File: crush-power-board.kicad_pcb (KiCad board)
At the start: 4 copper layers, 105 parts, among them J1 XT90PW-F, J2 1x2 Header, J3 Molex Micro Fit 3.0, J4 Barrel_Jack, J5 2157601008, U1 BD9G341AEFJ, U2 SIC461ED-T1-GE3, U3 SIC461ED-T1-GE3, U4 BD9G341AEFJ

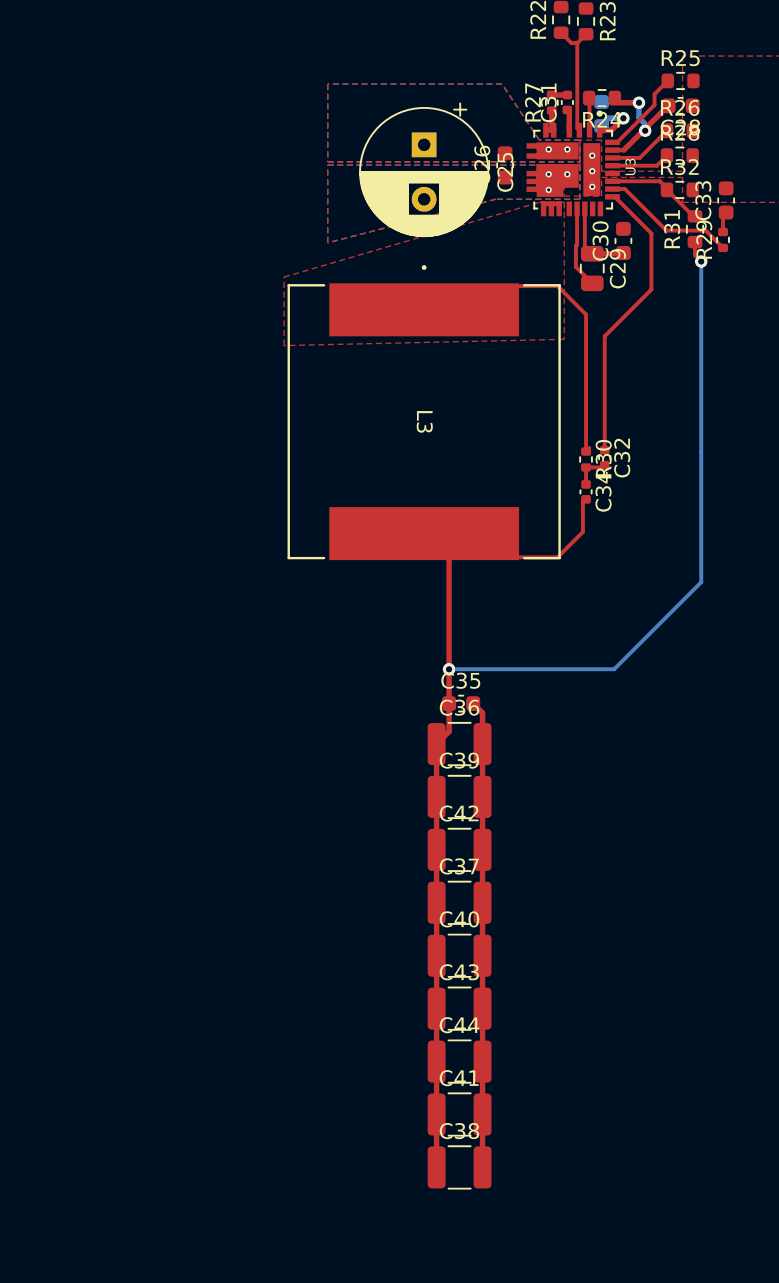
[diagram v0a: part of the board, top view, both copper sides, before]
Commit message: Added more vias and plane differences to 5V reg
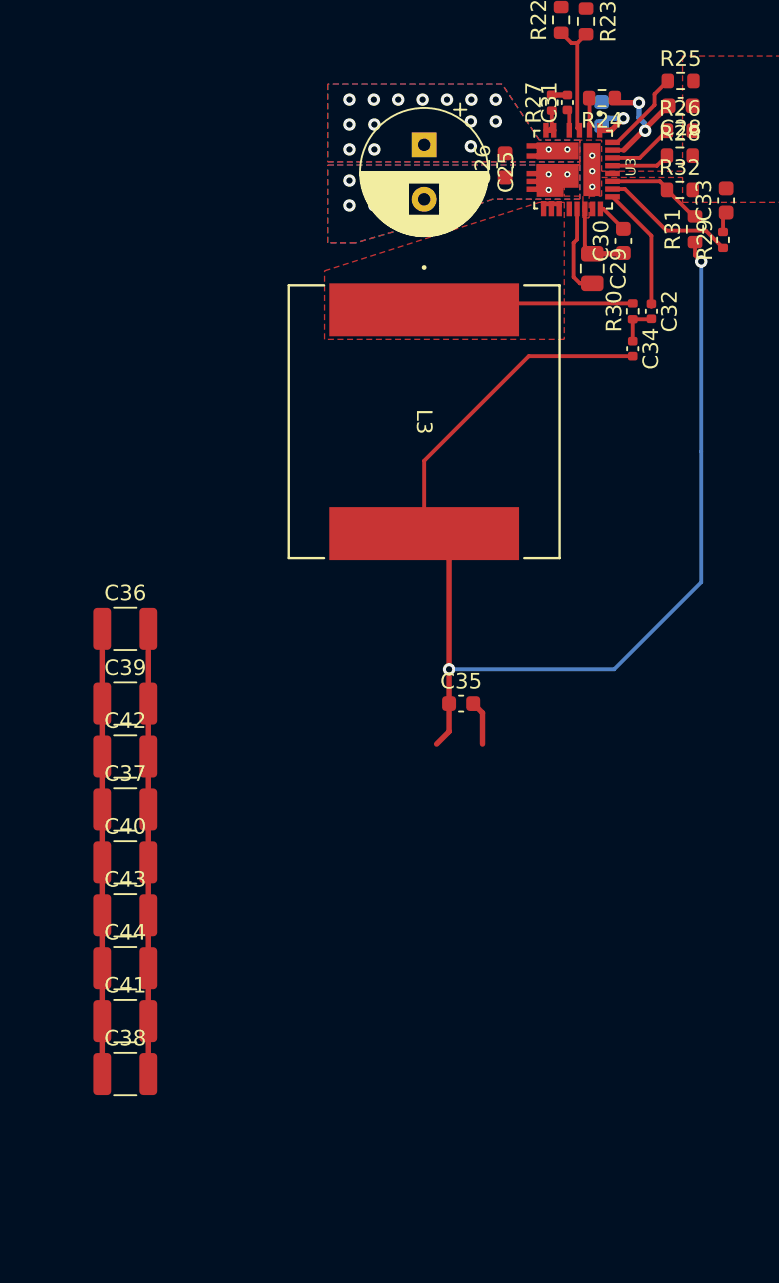
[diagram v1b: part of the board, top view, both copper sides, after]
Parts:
- moved C36 22.7 mm to (119.4, 105.0)
- moved C44 22.3 mm to (119.4, 126.8)
- moved C37 22.3 mm to (119.4, 116.6)
- moved C38 22.3 mm to (119.4, 133.6)
- moved C39 22.3 mm to (119.4, 109.8)
- moved C40 22.3 mm to (119.4, 120.0)
- moved C41 22.3 mm to (119.4, 130.2)
- moved C42 22.3 mm to (119.4, 113.2)
- moved C43 22.3 mm to (119.4, 123.4)
- moved R30 9.98 mm to (152.0, 84.6)
- moved C32 9.87 mm to (153.2, 84.6)
- moved C34 9.68 mm to (152.0, 87.0)
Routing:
- net Net-(U3-VSNS): track 18.6 -> 8.11 mm
- net 5V: track 96.1 -> 103.4 mm
- net Net-(L3-Pad1): track 20.7 -> 13.6 mm
- net Net-(U3-SS): track 0.00 -> 2.01 mm
- net Net-(U3-VDRV): track 5.25 -> 5.84 mm
- net GND: vias 31 -> 37
- net +BATT: vias 4 -> 18

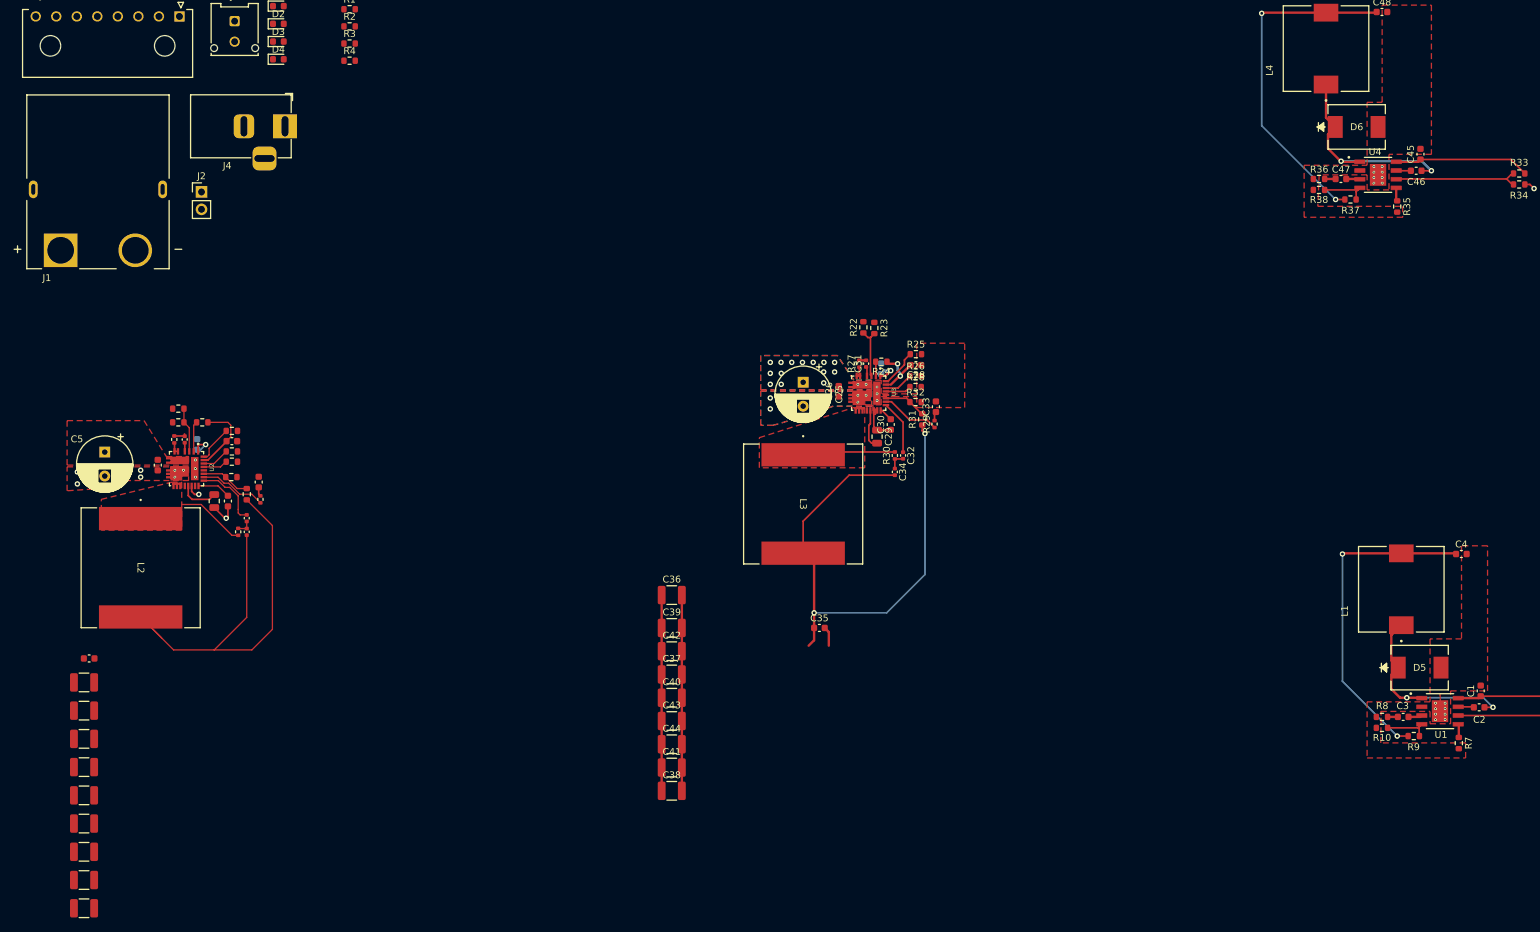
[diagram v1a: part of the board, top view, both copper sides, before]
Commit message: start 12v routing
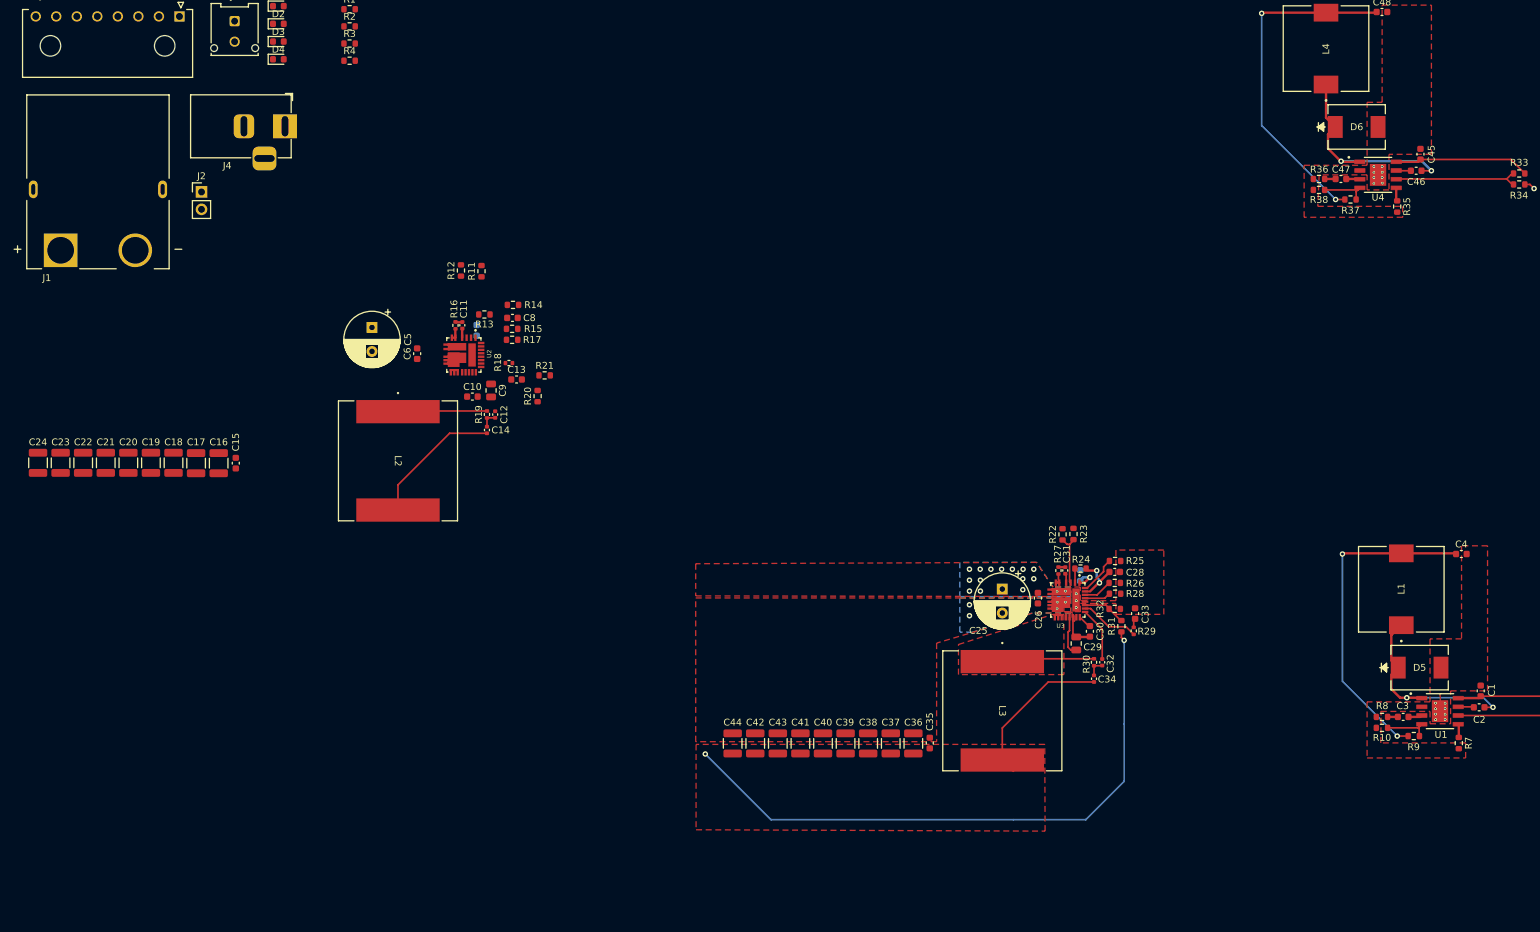
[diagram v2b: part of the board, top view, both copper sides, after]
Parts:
- moved C22 65.1 mm to (33.4, 85.7), turned to 90 degrees
- moved C23 61.1 mm to (30.1, 85.7), turned to 90 degrees
- moved C24 57.2 mm to (26.8, 85.7), turned to 90 degrees
- moved C19 53.6 mm to (43.3, 85.7), turned to 90 degrees
- moved R11 49.5 mm to (91.6, 57.7), turned to 90 degrees
- moved C20 49.0 mm to (40.0, 85.7), turned to 90 degrees
- moved R21 48.1 mm to (100.8, 72.9)
- moved R12 46.0 mm to (88.6, 57.6), turned to 90 degrees
- moved R14 45.0 mm to (96.2, 62.6)
- moved R20 44.9 mm to (99.8, 75.9)
- moved C16 44.8 mm to (53.2, 85.7), turned to 90 degrees
- moved C8 44.8 mm to (96.1, 64.5)
- moved R15 44.7 mm to (96.1, 66.1)
- moved R17 44.7 mm to (96.1, 67.7)
- moved C21 44.6 mm to (36.7, 85.7), turned to 90 degrees
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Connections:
- U1 pad 9: GND -> (no net)
- U4 pad 9: GND1 -> (no net)
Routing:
- net 12V: track 66.0 -> 19.8 mm
- net GND: track 47.4 -> 10.9 mm, vias 37 -> 21
- net Net-(U2-VDD): track 10.6 -> 0.00 mm
- net Net-(U2-COMP): track 9.83 -> 0.00 mm
- net Net-(U2-VSNS): track 9.81 -> 0.00 mm
- net 5V: track 103.4 -> 112.9 mm
- net Net-(U2-VFB): track 7.17 -> 0.00 mm
- net Net-(U2-EN): track 6.56 -> 0.00 mm
- net Net-(U2-Mode): track 5.74 -> 0.00 mm
- net Net-(U2-VDRV): track 5.73 -> 0.00 mm
- net Net-(U2-SS): track 4.89 -> 0.00 mm
- net Net-(U2-PGOOD): track 4.42 -> 0.00 mm
- net Net-(L2-Pad1): track 10.1 -> 14.4 mm
- net Net-(U2-Ilimit): track 4.01 -> 0.00 mm
- net +BATT: track 24.3 -> 20.6 mm, vias 18 -> 17
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- added copper zone on F.Cu, net 5V
- removed copper zone on F.Cu, net Net-(L2-Pad1)

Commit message: run drc
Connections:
- U1 pad 9: (no net) -> GND
- U2 pad 14.1: (no net) -> Net-(L2-Pad1)
- U3 pad 14.1: (no net) -> Net-(L3-Pad1)
- U4 pad 9: (no net) -> GND1
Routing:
- net Net-(D5-K): track 30.2 -> 32.0 mm
- net (no net): track 1.00 -> 0.00 mm
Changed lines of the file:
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@@
       (net 1 "+BATT") (pinfunction "VCC") (pintype "power_in"))
     (pad "9" smd rect (at 0 0) (size 2.4 3.2) (layers "F.Cu" "F.Mask")
-      (zone_connect 2))
+      (net 2 "GND") (zone_connect 2))
   )
   (footprint "Resistor_SMD:R_0603_1608Metric" (layer "F.Cu")
@@
     (pad "14" smd rect (at 2.525 0.9 90) (size 0.95 0.35) (layers "F.Cu" "F.Paste" "F.Mask")
       (net 36 "Net-(L3-Pad1)") (pinfunction "SW") (pintype "unspecified") (zone_connect 2))
-    (pad "14.1" smd rect (at 2.2 1.4 180) (size 1.35 0.3) (layers "F.Cu" "F.Paste" "F.Mask"))
+    (pad "14.1" smd rect (at 2.2 1.4 180) (size 1.35 0.3) (layers "F.Cu" "F.Paste" "F.Mask")
+      (net 36 "Net-(L3-Pad1)") (zone_connect 2))
     (pad "15" smd rect (at 2.525 0.25 90) (size 0.95 0.35) (layers "F.Cu" "F.Paste" "F.Mask")
       (net 61 "unconnected-(U3-GL-Pad15)") (pinfunction "GL") (pintype "unspecified+no_connect"))
@@
     (pad "14" smd rect (at 2.525 0.9 90) (size 0.95 0.35) (layers "F.Cu" "F.Paste" "F.Mask")
       (net 35 "Net-(L2-Pad1)") (pinfunction "SW") (pintype "unspecified"))
-    (pad "14.1" smd rect (at 2.2 1.4 180) (size 1.35 0.3) (layers "F.Cu" "F.Paste" "F.Mask"))
+    (pad "14.1" smd rect (at 2.2 1.4 180) (size 1.35 0.3) (layers "F.Cu" "F.Paste" "F.Mask")
+      (net 35 "Net-(L2-Pad1)") (zone_connect 2))
     (pad "15" smd rect (at 2.525 0.25 90) (size 0.95 0.35) (layers "F.Cu" "F.Paste" "F.Mask")
       (net 59 "unconnected-(U2-GL-Pad15)") (pinfunction "GL") (pintype "unspecified+no_connect"))
@@
       (net 63 "+BATT_T") (pinfunction "VCC") (pintype "power_in"))
     (pad "9" smd rect (at 0 0) (size 2.4 3.2) (layers "F.Cu" "F.Mask")
-      (zone_connect 2))
+      (net 64 "GND1") (zone_connect 2))
   )
   (footprint "Connector_Molex:Molex_Micro-Fit_3.0_43045-0212_2x01_P3.00mm_Vertical" (layer "F.Cu")
@@
     )
   )
-  (segment (start 250.6 124) (end 250.6 123.6) (width 0) (layer "F.Cu") (net 0))
-  (segment (start 251.2 124) (end 250.6 124) (width 0) (layer "F.Cu") (net 0))
   (segment (start 180.5 102.4197) (end 180.3 102.6197) (width 0.35) (layer "F.Cu") (net 1))
   (segment (start 247.825 119.775) (end 250.05 122) (width 0.25) (layer "F.Cu") (net 1))
@@
   (segment (start 234.31 121.33) (end 236.53 121.33) (width 0.25) (layer "F.Cu") (net 3))
   (segment (start 236.53 121.33) (end 236.6 121.4) (width 0.25) (layer "F.Cu") (net 3))
-  (segment (start 224.5376 114.586) (end 224.5376 110.8624) (width 0.35) (layer "F.Cu") (net 4))
+  (segment (start 224.5376 114.586) (end 224.5376 110.8624) (width 0.25) (layer "F.Cu") (net 4))
+  (segment (start 225.741712 120) (end 224.2 118.458288) (width 0.35) (layer "F.Cu") (net 4))
   (segment (start 224.5376 116.614) (end 225.5516 115.6) (width 0.25) (layer "F.Cu") (net 4))
   (segment (start 238.15 121.4) (end 239.4 121.4) (width 0.25) (layer "F.Cu") (net 4))
-  (segment (start 225.812422 120) (end 224.5376 118.725178) (width 0.35) (layer "F.Cu") (net 4))
+  (segment (start 224.5376 110.8624) (end 226 109.4) (width 0.25) (layer "F.Cu") (net 4))
   (segment (start 225.5516 115.6) (end 224.5376 114.586) (width 0.25) (layer "F.Cu") (net 4))
+  (segment (start 224.2 116.9516) (end 225.5516 115.6) (width 0.35) (layer "F.Cu") (net 4))
   (segment (start 228.94 120) (end 229 120.06) (width 0.25) (layer "F.Cu") (net 4))
-  (segment (start 226.8 120) (end 225.812422 120) (width 0.35) (layer "F.Cu") (net 4))
+  (segment (start 224.2 118.458288) (end 224.2 116.9516) (width 0.35) (layer "F.Cu") (net 4))
+  (segment (start 226.8 120) (end 225.741712 120) (width 0.35) (layer "F.Cu") (net 4))
   (segment (start 226.8 120) (end 228.94 120) (width 0.35) (layer "F.Cu") (net 4))
-  (segment (start 224.5376 118.725178) (end 224.5376 116.614) (width 0.35) (layer "F.Cu") (net 4))
-  (segment (start 224.5376 110.8624) (end 226 109.4) (width 0.35) (layer "F.Cu") (net 4))
   (via (at 239.4 121.4) (size 0.8) (drill 0.4) (layers "F.Cu" "B.Cu") (net 4))
   (via (at 226.8 120) (size 0.8) (drill 0.4) (layers "F.Cu" "B.Cu") (net 4))

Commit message: finish main 12v layout
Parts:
- moved C15 167.6 mm to (223.0, 75.4)
- moved C16 167.6 mm to (220.5, 75.4)
- moved C18 167.6 mm to (213.9, 75.3)
- moved C19 167.6 mm to (210.6, 75.3)
- moved C20 167.6 mm to (207.3, 75.3)
- moved C21 167.6 mm to (204.0, 75.3)
- moved C23 167.6 mm to (197.4, 75.3)
- moved C17 167.6 mm to (217.2, 75.4)
- moved C22 167.6 mm to (200.7, 75.3)
- moved C24 167.6 mm to (194.1, 75.3)
- moved R18 157.6 mm to (252.8, 59.7), turned to 90 degrees
- moved C6 157.1 mm to (238.6, 54.5)
- moved C13 156.9 mm to (252.8, 57.1), turned to 90 degrees
- moved C12 156.9 mm to (249.8, 63.6)
- moved C14 156.9 mm to (248.6, 65.9)
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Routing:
- net 12V: track 19.8 -> 104.6 mm, vias 0 -> 2
- net Net-(U2-COMP): track 0.00 -> 9.21 mm
- net Net-(U2-VDD): track 0.00 -> 9.12 mm, vias 0 -> 2
- net Net-(U2-VSNS): track 0.00 -> 8.39 mm
- net Net-(U2-EN): track 0.00 -> 8.31 mm
- net Net-(U2-VFB): track 0.00 -> 6.37 mm
- net Net-(U2-Mode): track 0.00 -> 5.64 mm
- net Net-(U2-VDRV): track 0.00 -> 5.02 mm
- net Net-(U2-Ilimit): track 0.00 -> 4.57 mm
- net Net-(U2-fsw): track 0.00 -> 4.12 mm
- net +BATT: track 20.6 -> 24.0 mm, vias 17 -> 20
- net Net-(U2-PGOOD): track 0.00 -> 2.69 mm
- net Net-(L2-Pad1): track 14.4 -> 16.9 mm
- net Net-(U2-SS): track 0.00 -> 1.87 mm
- net Net-(C13-Pad1): track 0.00 -> 1.30 mm
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- added copper zone on F.Cu, net 12V
- added copper zone on F.Cu, net Net-(L2-Pad1)
